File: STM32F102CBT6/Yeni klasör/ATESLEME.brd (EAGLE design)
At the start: 35.3 x 57.9 mm, 55 parts, among them U1 ADXL345PATRICK, U3 AMS1117-3.3, U4 STM32F102CBT6, Y2 ABM2B-8.000MHZ-10-1-U-T

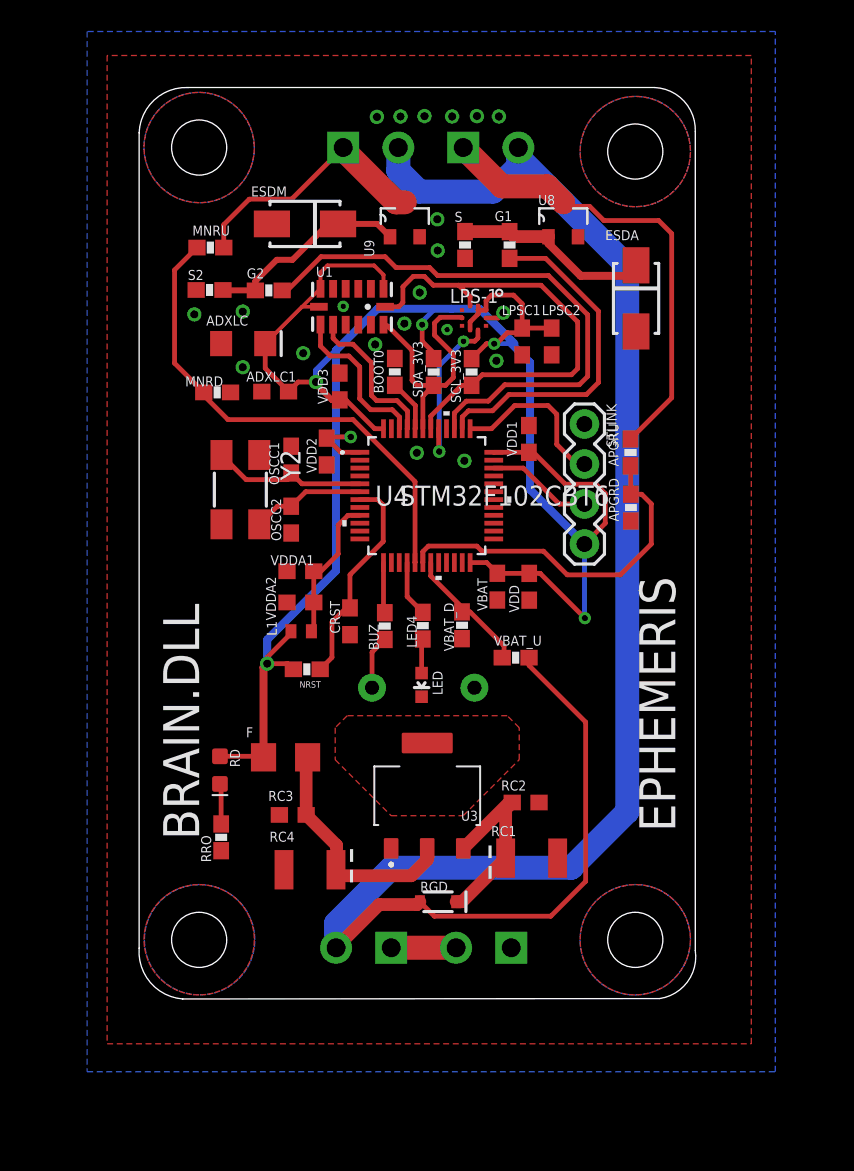
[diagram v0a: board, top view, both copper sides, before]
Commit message: NMOS trace was be expanded and 1206 package version was created
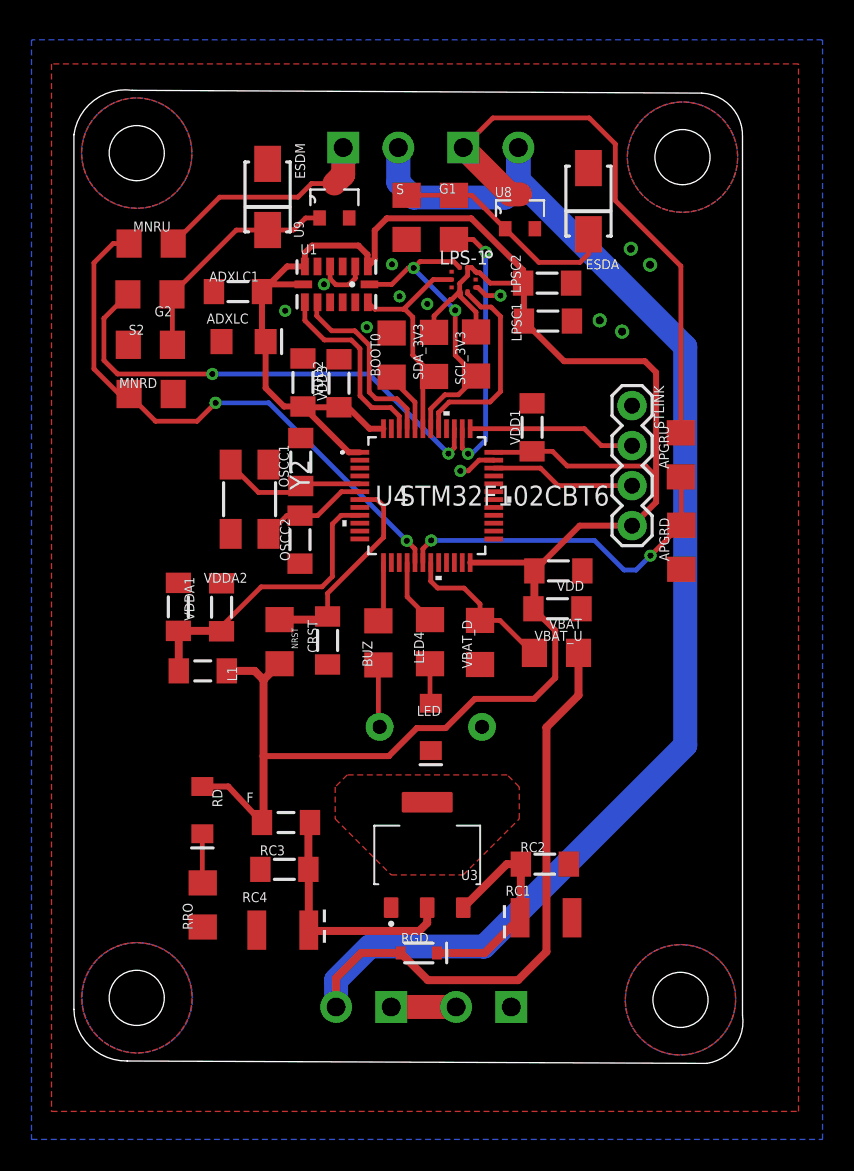
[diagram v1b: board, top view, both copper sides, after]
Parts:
- ADXLC1, CRST, LPSC1, LPSC2, OSCC1, OSCC2, RC2, RC3, VBAT, VDD, VDD1, VDD2, VDD3, VDDA1, VDDA2: device SparkFun-Capacitors:0603 -> 52101-101-REV-A_v16:RC-MASTER-SMD_C1206MP
- APGRD, MNRD, S, S2, VBAT_D: value 3.3k -> 3k3; device SparkFun-Resistors:0603-RES -> SparkFun-Resistors:1206
- APGRU, BOOT0, G1, G2, LED4, MNRU, NRST, VBAT_U: device SparkFun-Resistors:0603-RES -> SparkFun-Resistors:1206
- BUZ: value 22R -> 22; device SparkFun-Resistors:0603-RES -> SparkFun-Resistors:1206
- F: device SparkFun-Fuses:1206 -> 52101-101-REV-A_v16:RC-MASTER-SMD_L1206MP
- L1: value BLM15HB221SN1 -> (none); device inductors:0402 -> 52101-101-REV-A_v16:RC-MASTER-SMD_L1206MP
- LED, RD: device SparkFun-LED:LED-0603 -> SparkFun-LED:LED-1206
- RRO: value 1.5k -> 330; device SparkFun-Resistors:0603-RES -> SparkFun-Resistors:1206
- SCL_3V3, SDA_3V3: value 4.7k -> 4k7; device SparkFun-Resistors:0603-RES -> SparkFun-Resistors:1206
- moved VDDA1 8.07 mm to (-3.68, 31.4), turned to 90 degrees
- moved G2 7.55 mm to (-5.49, 51.2), turned to 180 degrees
- moved ESDA 6.87 mm to (22.4, 57.1), turned to 90 degrees
- moved ADXLC1 6.78 mm to (0.10, 51.4)
- moved L1 6.74 mm to (-2.13, 27.3), turned to 180 degrees
- moved S2 5.12 mm to (-5.46, 48.0)
- moved VDDA2 5.01 mm to (-0.94, 31.4), turned to 90 degrees
- moved VDD2 4.63 mm to (4.23, 45.6), turned to 90 degrees
- moved U9 4.63 mm to (6.22, 57.2)
- moved RRO 4.45 mm to (-2.13, 12.5)
- moved RC4 4.21 mm to (2.95, 10.9)
- moved MNRD 4.19 mm to (-5.41, 44.9)
- moved F 4.14 mm to (3.15, 17.7)
- moved S 4.10 mm to (10.8, 56.1)
- moved RC2 4.10 mm to (19.6, 15.1)
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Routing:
- net SCL_3V3: track 30.8 -> 20.0 mm, vias 0 -> 2
- net VDDA: track 9.34 -> 19.3 mm
- net VIN: track 113.5 -> 122.4 mm
- net 3.3V: track 142.0 -> 149.3 mm, vias 6 -> 0
- net GND: track 1.24 -> 7.66 mm, vias 21 -> 12
- net VAPG: track 29.6 -> 36.0 mm
- net MN: track 36.1 -> 30.9 mm, vias 0 -> 2
- net VMNS: track 31.6 -> 36.4 mm, vias 0 -> 2
- net APG: track 21.9 -> 17.5 mm, vias 0 -> 2
- net SWDIO: track 6.70 -> 9.24 mm
- net INT1: track 10.6 -> 13.1 mm, vias 2 -> 0
- net N$14: track 12.6 -> 14.8 mm
- net IN2: track 9.85 -> 12.1 mm
- net VMN: track 16.5 -> 14.3 mm
- net VNR: track 12.3 -> 14.4 mm
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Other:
- board size 35.3 x 57.9 mm -> 42.5 x 61.8 mm
